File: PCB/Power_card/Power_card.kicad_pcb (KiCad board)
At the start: 2 copper layers, 61.2 x 71.6 mm, 55 parts, among them J1 Conn_01x01_Pin, J2 Conn_01x01_Pin, J3 Conn_01x01_Pin, J4 Conn_01x01_Pin, J5 Conn_01x01_Pin, J6 Conn_01x01_Pin, J7 Conn_02x04_Counter_Clockwise, J8 Conn_01x01_Pin, K1 Relay_SPST-NO, K2 Relay_SPST-NO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

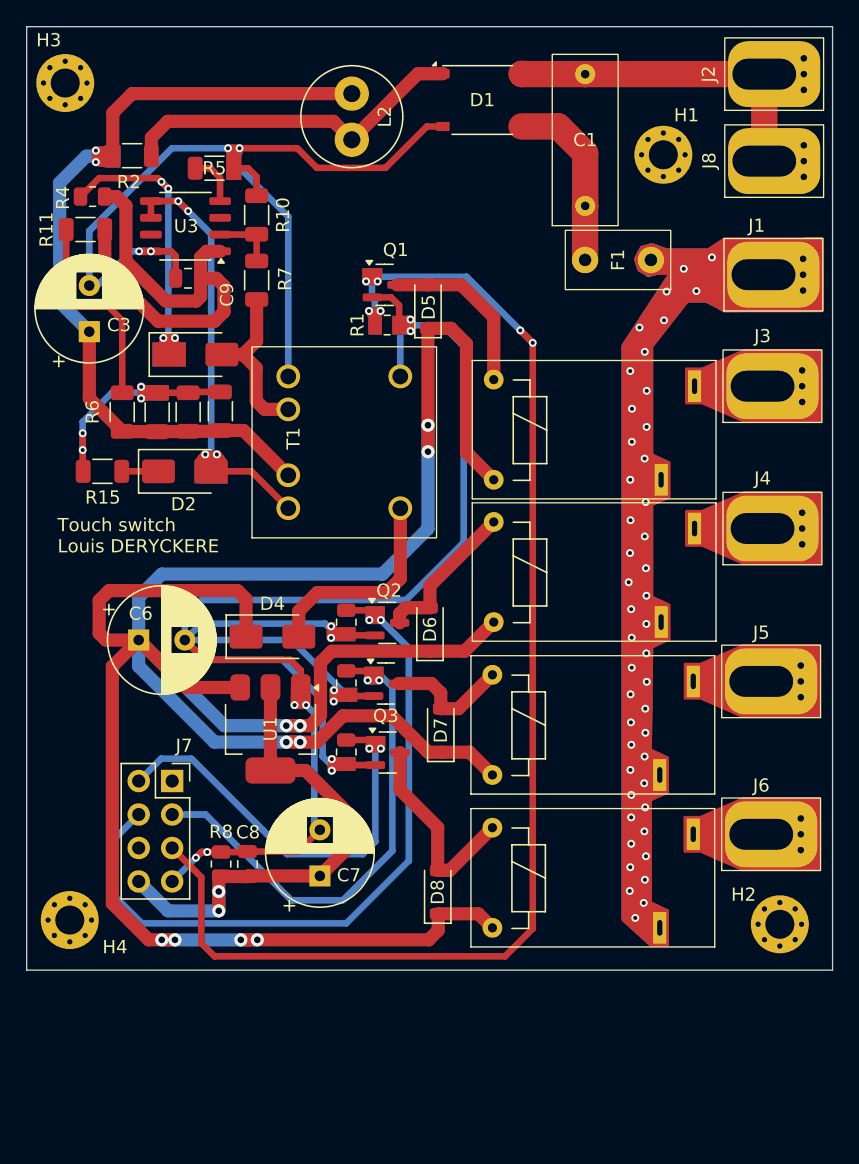
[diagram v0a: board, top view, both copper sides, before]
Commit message: Projet renommé
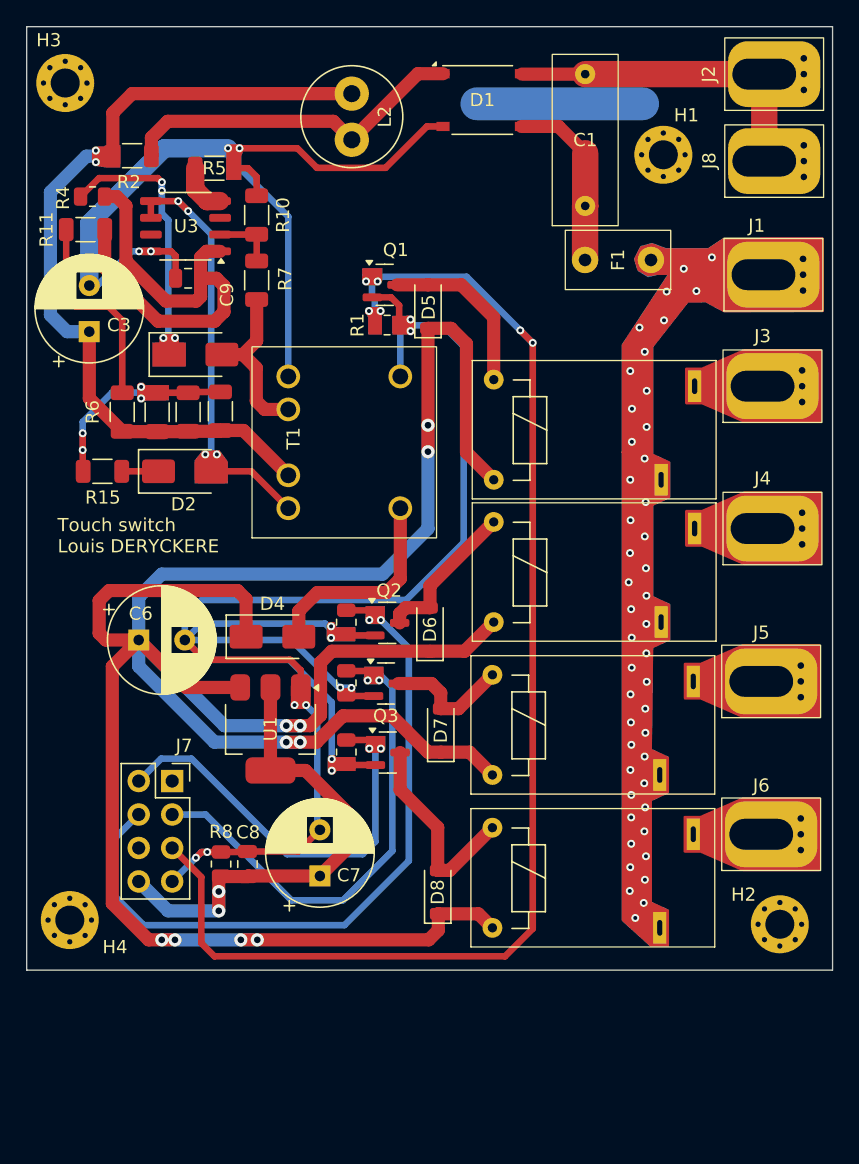
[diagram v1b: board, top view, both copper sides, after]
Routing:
- net +310VDC: track 61.4 -> 63.0 mm
- net GND2: track 137.8 -> 139.0 mm
- net Net-(D3-K): track 20.6 -> 19.9 mm

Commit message: Routage
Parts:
- moved H4 11.8 mm to (113.4, 93.9)
- moved J7 4.51 mm to (108.8, 94.1)
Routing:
- net +5VDC: track 214.9 -> 221.9 mm
- net CT4: track 31.4 -> 36.0 mm
- net GND2: track 139.0 -> 143.6 mm
- net +3.3V: track 38.0 -> 42.4 mm
- net CT2: track 53.7 -> 57.8 mm
- net CT3: track 36.8 -> 39.0 mm
- net CT1: track 98.4 -> 97.7 mm
- net Net-(D3-K): track 19.9 -> 20.5 mm

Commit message: Ajout des touch switch
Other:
- board text added: "Touch switch Power card lsdrckr"
- board text removed: "Touch switch Louis DERYCKERE"
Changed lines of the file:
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@@
 		(layer "Edge.Cuts")
 	)
-	(gr_text "Touch switch\nLouis DERYCKERE"
-		(at 103.59 74.02 0)
+	(gr_text "Touch switch\nPower card\nlsdrckr"
+		(at 130.19 49.51 0)
 		(layer "F.SilkS")
 		(effects

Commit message: Changement de connecteurs
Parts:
- J7: footprint Connector_PinSocket_2.54mm:PinSocket_2x04_P2.54mm_Vertical -> Touch_Switch_Custom:Pin femelle
- moved J7 7.29 mm to (111.7, 100.9), turned to 180 degrees
- moved H4 3.86 mm to (112.3, 90.2)
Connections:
- J7 pad 1: unconnected-(J7-Pin_1-Pad1) -> +3.3V
- J7 pad 2: CT4 -> CT1
- J7 pad 4: CT2 -> GND2
- J7 pad 5: CT1 -> CT4
- J7 pad 7: GND2 -> unconnected-(J7-Pin_7-Pad7)
- J7 pad 8: +3.3V -> CT2
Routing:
- net +3.3V: track 42.4 -> 34.7 mm
- net GND2: track 143.6 -> 137.7 mm, vias 12 -> 10
- net CT1: track 97.7 -> 92.8 mm, vias 6 -> 10
- net CT2: track 57.8 -> 53.3 mm, vias 2 -> 4
- net CT3: track 39.0 -> 36.7 mm, vias 2 -> 4
- net CT4: track 36.0 -> 36.9 mm, vias 2 -> 4

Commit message: Ajout des footprints
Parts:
- J7: footprint Touch_Switch_Custom:Pin femelle -> Touch_Switch_Custom:PinFemelle
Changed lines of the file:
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@@
 		)
 	)
-	(footprint "Touch_Switch_Custom:Pin femelle"
+	(footprint "Touch_Switch_Custom:PinFemelle"
 		(layer "F.Cu")
 		(at 111.65 100.86 180)
 		(property "Reference" "J7"
-			(at 1.5 -3.65 180)
+			(at 0 -16.4 180)
 			(unlocked yes)
 			(layer "F.SilkS")
@@
 			)
 		)
-		(property "Footprint" "Touch_Switch_Custom:Pin femelle"
+		(property "Footprint" "Touch_Switch_Custom:PinFemelle"
 			(at 0 -15.9 180)
 			(unlocked yes)

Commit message: Rota IC contrôle
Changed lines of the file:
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@@
 		(at 111.65 100.86 180)
 		(property "Reference" "J7"
-			(at 0 -16.4 180)
+			(at -2.1 5.9 0)
 			(unlocked yes)
 			(layer "F.SilkS")
